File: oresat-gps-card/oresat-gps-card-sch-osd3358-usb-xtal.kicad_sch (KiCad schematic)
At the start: 42 parts, among them J2 FTSH-105-XX-X-DV-K, U1 OSD3358-512M-BSM, U11 RCLAMP0504FB, U12 TPS2051CDBVR, Y1 24MHz, Y2 Crystal

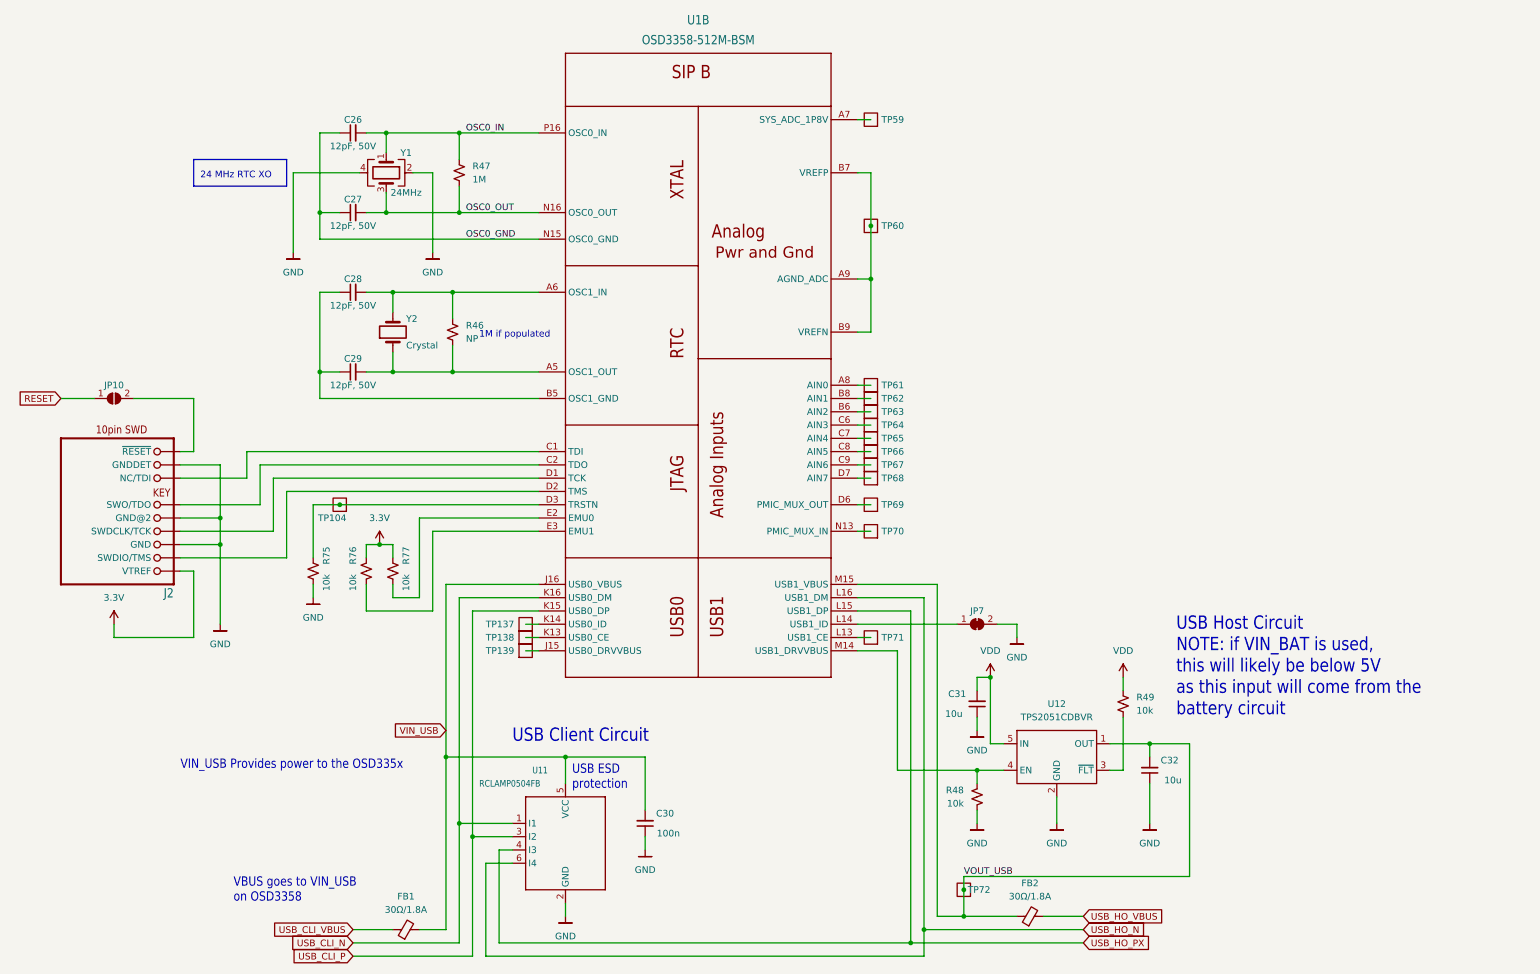
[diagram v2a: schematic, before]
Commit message: Updated GPS card with changes from C3 and notes. Fixed library issues
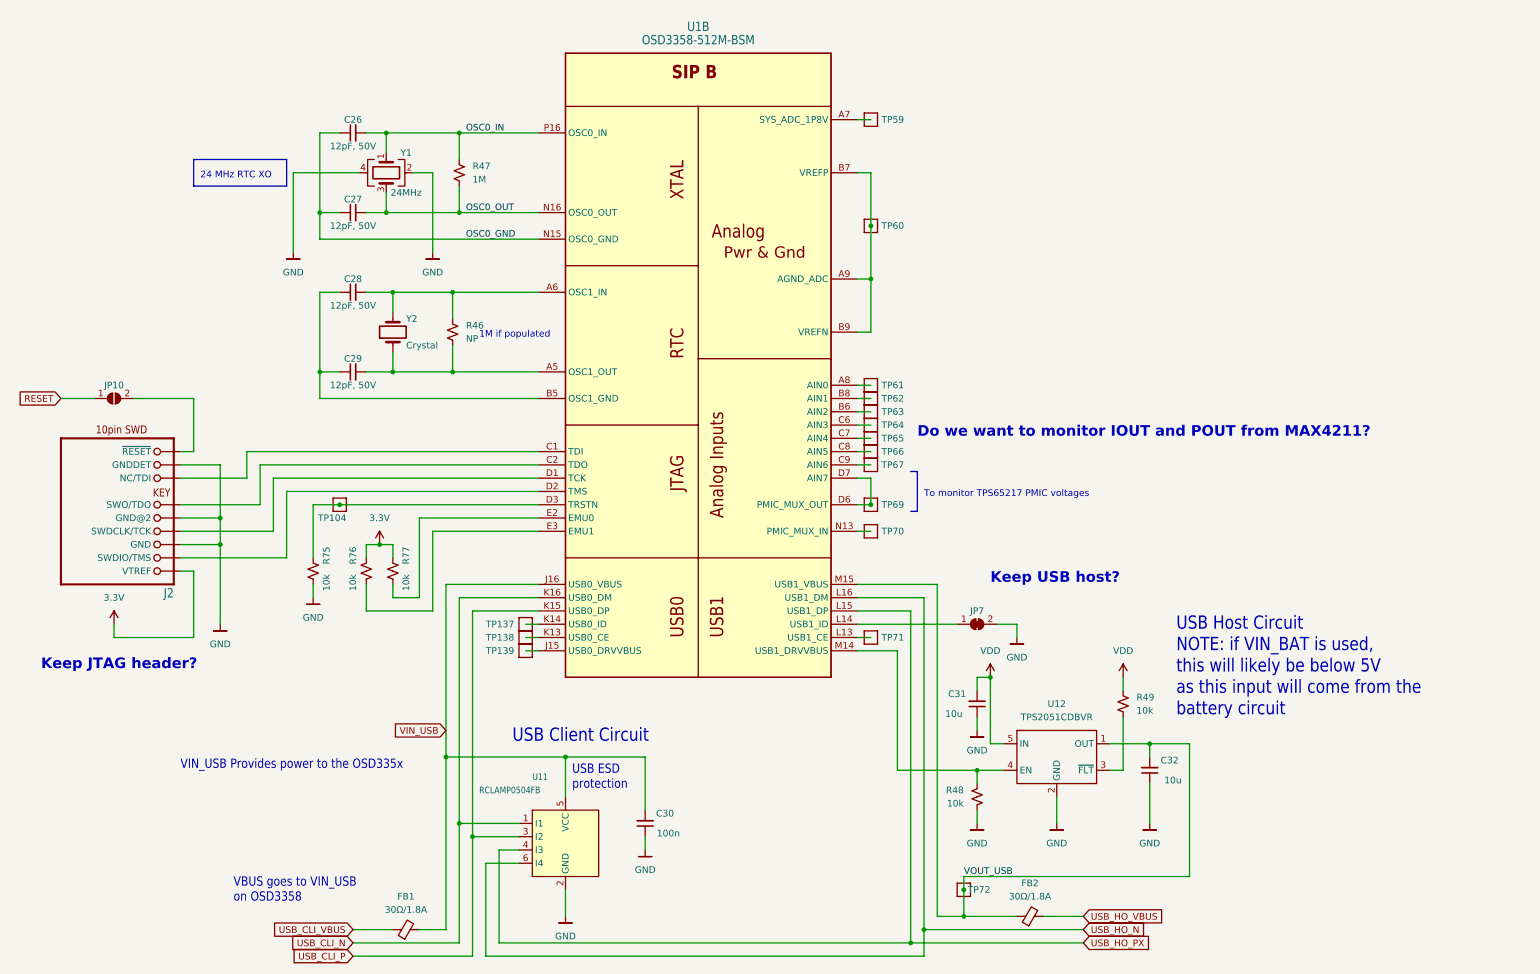
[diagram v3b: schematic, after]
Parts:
- removed TP68: Test-Point, OreSat-TestPoint:PAD.03X.04, symbol OreSat-TestPoint:Test-Point
- J2: symbol J-Samtec-FTSH-105-XX-X-DV-K-jtag-connector:FTSH-105-XX-X-DV-K -> oresat-connectors:FTSH-105-XX-X-DV-K
- TP104, TP137, TP138, TP139, TP59, TP60, TP61, TP62, TP63, TP64, TP65, TP66, TP67, TP69, TP70, TP71, TP72: value Test-Point -> 0.03x0.04; footprint OreSat-TestPoint:PAD.03X.04 -> oresat-misc:TestPoint_Pad_D1.0mm; symbol OreSat-TestPoint:Test-Point -> oresat-misc:Test-Point-1mm-round
- U1: footprint oresat-footprints:U-Octavo-OSD335X-BGA-256 -> oresat-ics:U-Octavo-OSD335X-BGA-256; symbol U-OSD3358-512M-BSM:OSD3358-512M-BSM -> oresat-ics:OSD3358-512M-BSM
- U11: symbol U-Semtech-RCLAMP0504FB-tvs-diodes:RCLAMP0504FB -> oresat-ics:RCLAMP0504FB
- U12: symbol U-TI-TPS2051CDBVR-usb-power-switch:TPS2051CDBVR -> oresat-ics:TPS2051CDBVR
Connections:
- net at TP69.1, U1.D6 (PMIC_MUX_OUT): now also U1.D7 (AIN7)
- net VDD renamed 1.1V
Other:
- note added: "Do we want to monitor IOUT and POUT from MAX4211?"
- note added: "Keep JTAG header?"
- note added: "Keep USB host?"
- note added: "To monitor TPS65217 PMIC voltages"

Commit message: Updated GPS card
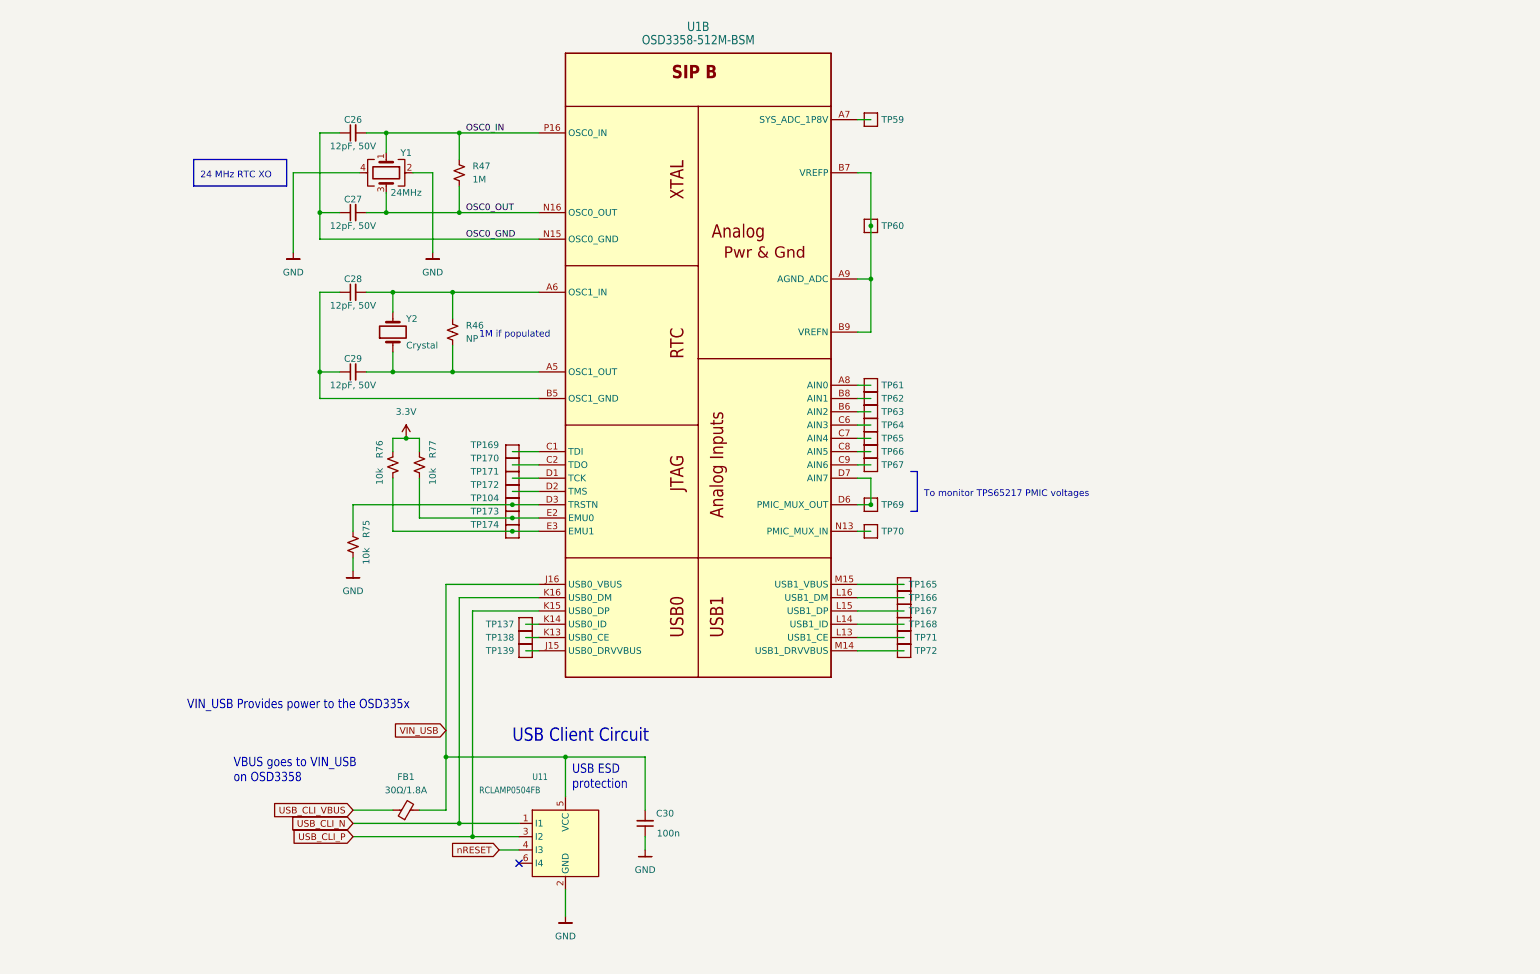
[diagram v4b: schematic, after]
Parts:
- removed C31, C32: 10u, Capacitor_SMD:C_0805_2012Metric, symbol Device:C_Small
- removed FB2: 30Ω/1.8A, Inductor_SMD:L_0603_1608Metric, symbol Device:FerriteBead_Small
- removed J2: FTSH-105-XX-X-DV-K, oresat-footprints:J-Samtec-CON10_2X5_DUK_FTSH, symbol oresat-connectors:FTSH-105-XX-X-DV-K
- removed JP10: SolderJumper_2_Open, oresat-footprints:SMT-JUMPER_2_NO_SILK, symbol Jumper:SolderJumper_2_Open
- removed JP7: SolderJumper_2_Bridged, oresat-footprints:SMT-JUMPER_2_NC_TRACE_SILK, symbol Jumper:SolderJumper_2_Bridged
- removed R48, R49: 10k, Resistor_SMD:R_0603_1608Metric, symbol Device:R_Small_US
- removed U12: TPS2051CDBVR, Package_TO_SOT_SMD:SOT-23-5, symbol oresat-ics:TPS2051CDBVR
- added TP165, TP166, TP167, TP168, TP169, TP170, TP171, TP172, TP173, TP174: 0.03x0.04, oresat-misc:TestPoint_Pad_D1.0mm, symbol oresat-misc:Test-Point-1mm-round
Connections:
- net at U1.D2 (TMS): now also TP172.1
- net at U1.D1 (TCK): now also TP171.1
- net at U1.C2 (TDO): now also TP170.1
- net at U1.C1 (TDI): now also TP169.1
- net at R76.2, U1.E3 (EMU1): now also TP174.1
- net at U1.L14 (USB1_ID): now also TP168.1
- net at U1.M14 (USB1_DRVVBUS): now also TP72.1
- net at R77.2, U1.E2 (EMU0): now also TP173.1
- net USB_HO_N: no longer names the net of U11.6 (I4)
- net USB_HO_N: no longer U1.L16 (USB1_DM)
- net USB_HO_PX: no longer names the net of U1.L15 (USB1_DP)
- net USB_HO_PX: now also TP167.1; no longer U11.4 (I3)
- net VOUT_USB: no longer names the net of U1.M15 (USB1_VBUS)
- net VOUT_USB: now also TP165.1; no longer TP72.1
- new net: TP166.1, U1.L16 (USB1_DM)
- new net nRESET: U11.4 (I3)
- no-connect marks 0 -> 1
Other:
- note removed: "Do we want to monitor IOUT and POUT from MAX4211?"
- note removed: "Keep JTAG header?"
- note removed: "Keep USB host?"
- note removed: "USB Host Circuit NOTE: if VIN_BAT is used, this will likely be below 5V as this input will come from the battery circuit"
- moved on the sheet: FB1, R75, R76, R77, TP104, TP71

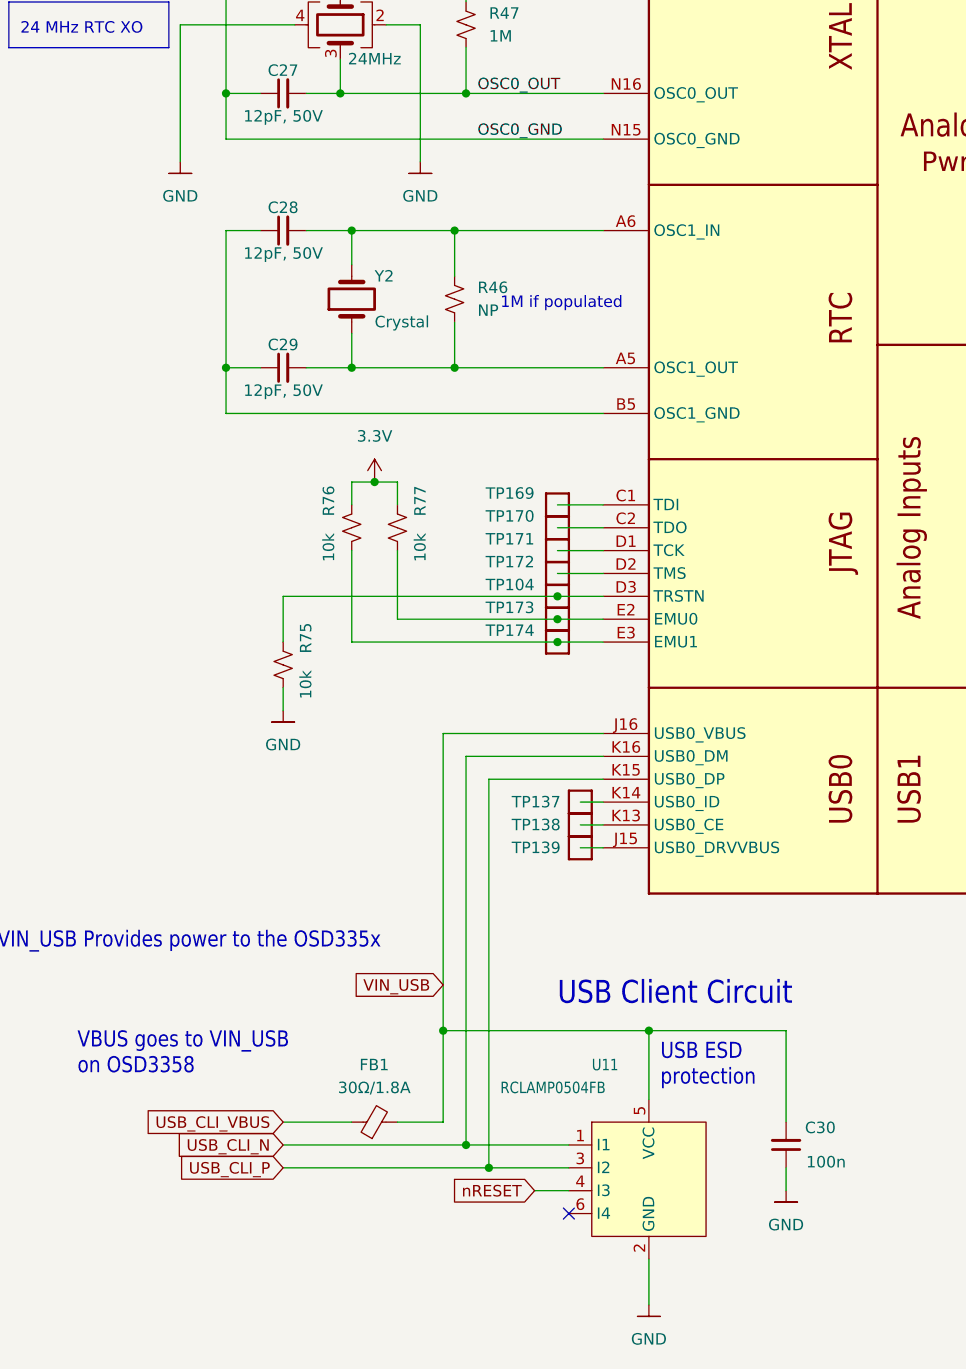
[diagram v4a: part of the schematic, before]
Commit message: Cleaned up ERC and DRC errors on GPS card
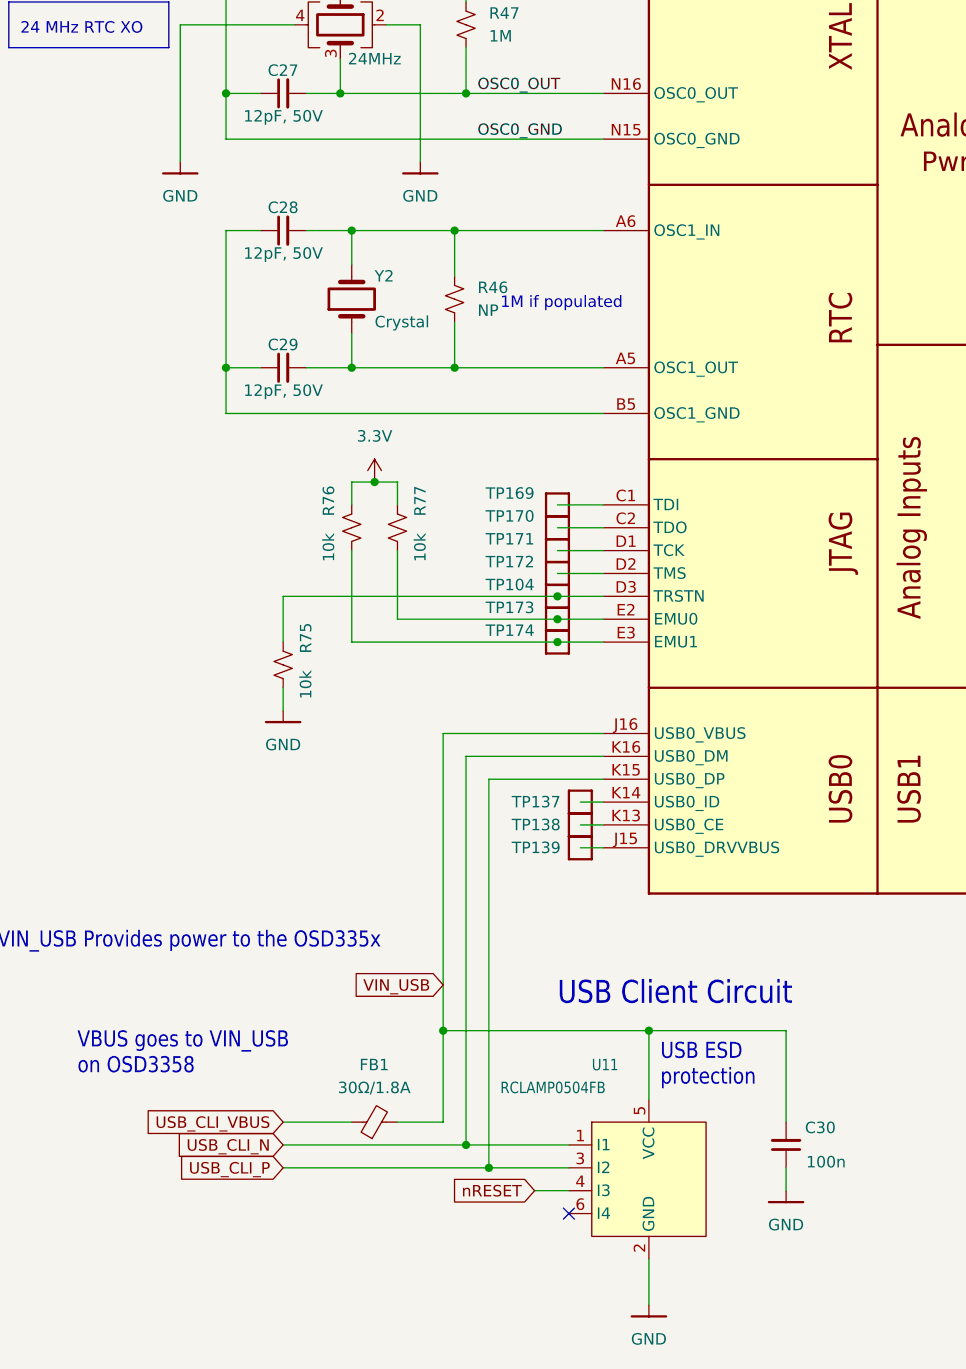
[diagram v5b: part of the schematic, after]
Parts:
- Y1: footprint oresat-footprints:CRYSTAL-5X3.2-4SMD -> oresat-misc:CRYSTAL-5X3.2-4SMD
- Y2: footprint oresat-footprints:CRYSTAL_3.2X1.5 -> oresat-misc:CRYSTAL_3.2X1.5
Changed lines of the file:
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@@
       (effects (font (size 1.27 1.27)))
     )
-    (property "Footprint" "oresat-footprints:CRYSTAL-5X3.2-4SMD" (at 125.73 71.12 0)
+    (property "Footprint" "oresat-misc:CRYSTAL-5X3.2-4SMD" (at 125.73 71.12 0)
       (effects (font (size 1.27 1.27)) hide)
     )
@@
       (effects (font (size 1.27 1.27)) (justify right))
     )
-    (property "Footprint" "oresat-footprints:CRYSTAL_3.2X1.5" (at 127 101.6 0)
+    (property "Footprint" "oresat-misc:CRYSTAL_3.2X1.5" (at 127 101.6 0)
       (effects (font (size 1.27 1.27)) hide)
     )

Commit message: Updated KiCAD 8, updated schematic sheet info, polished some schematic things, and made DNP parts DNP.
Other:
- title: (none) -> OreSat GPS Card
